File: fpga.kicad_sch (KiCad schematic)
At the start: 50 parts, among them U1 MACHXO2-1200HC-4TG100C, U2 TDC_7200, X1 16MHz

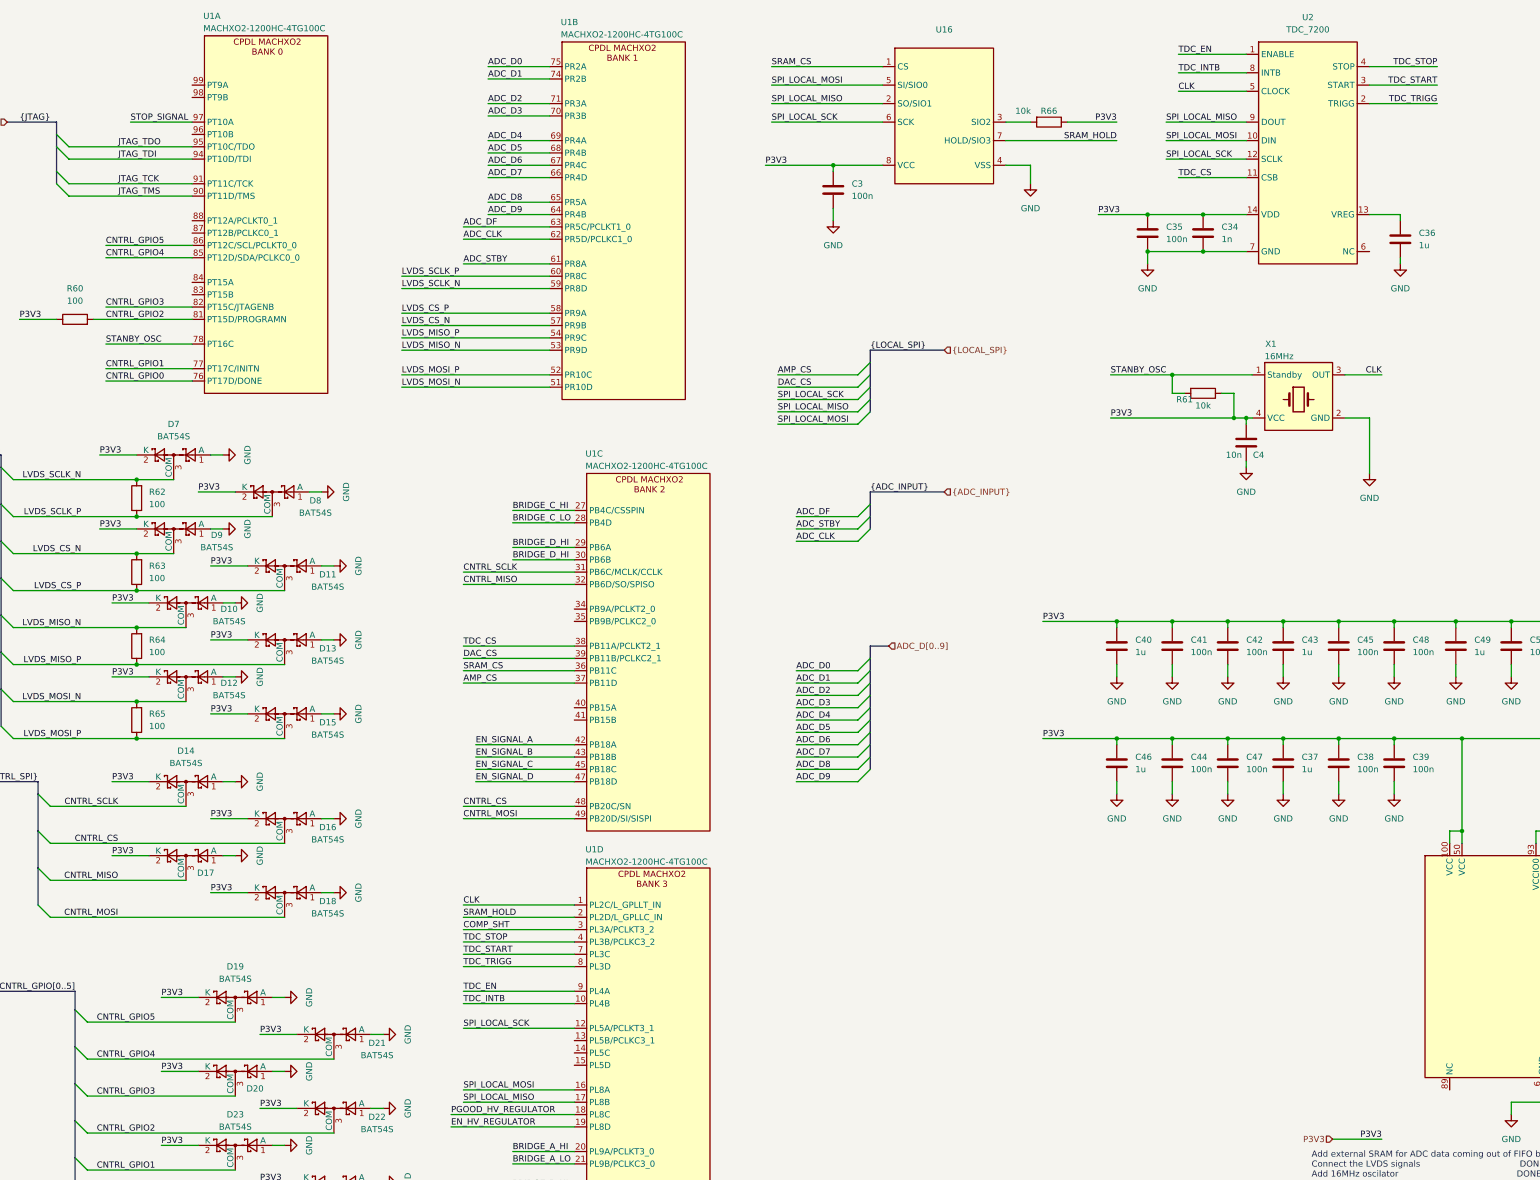
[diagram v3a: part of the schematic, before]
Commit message: schematic ready, basic layout done
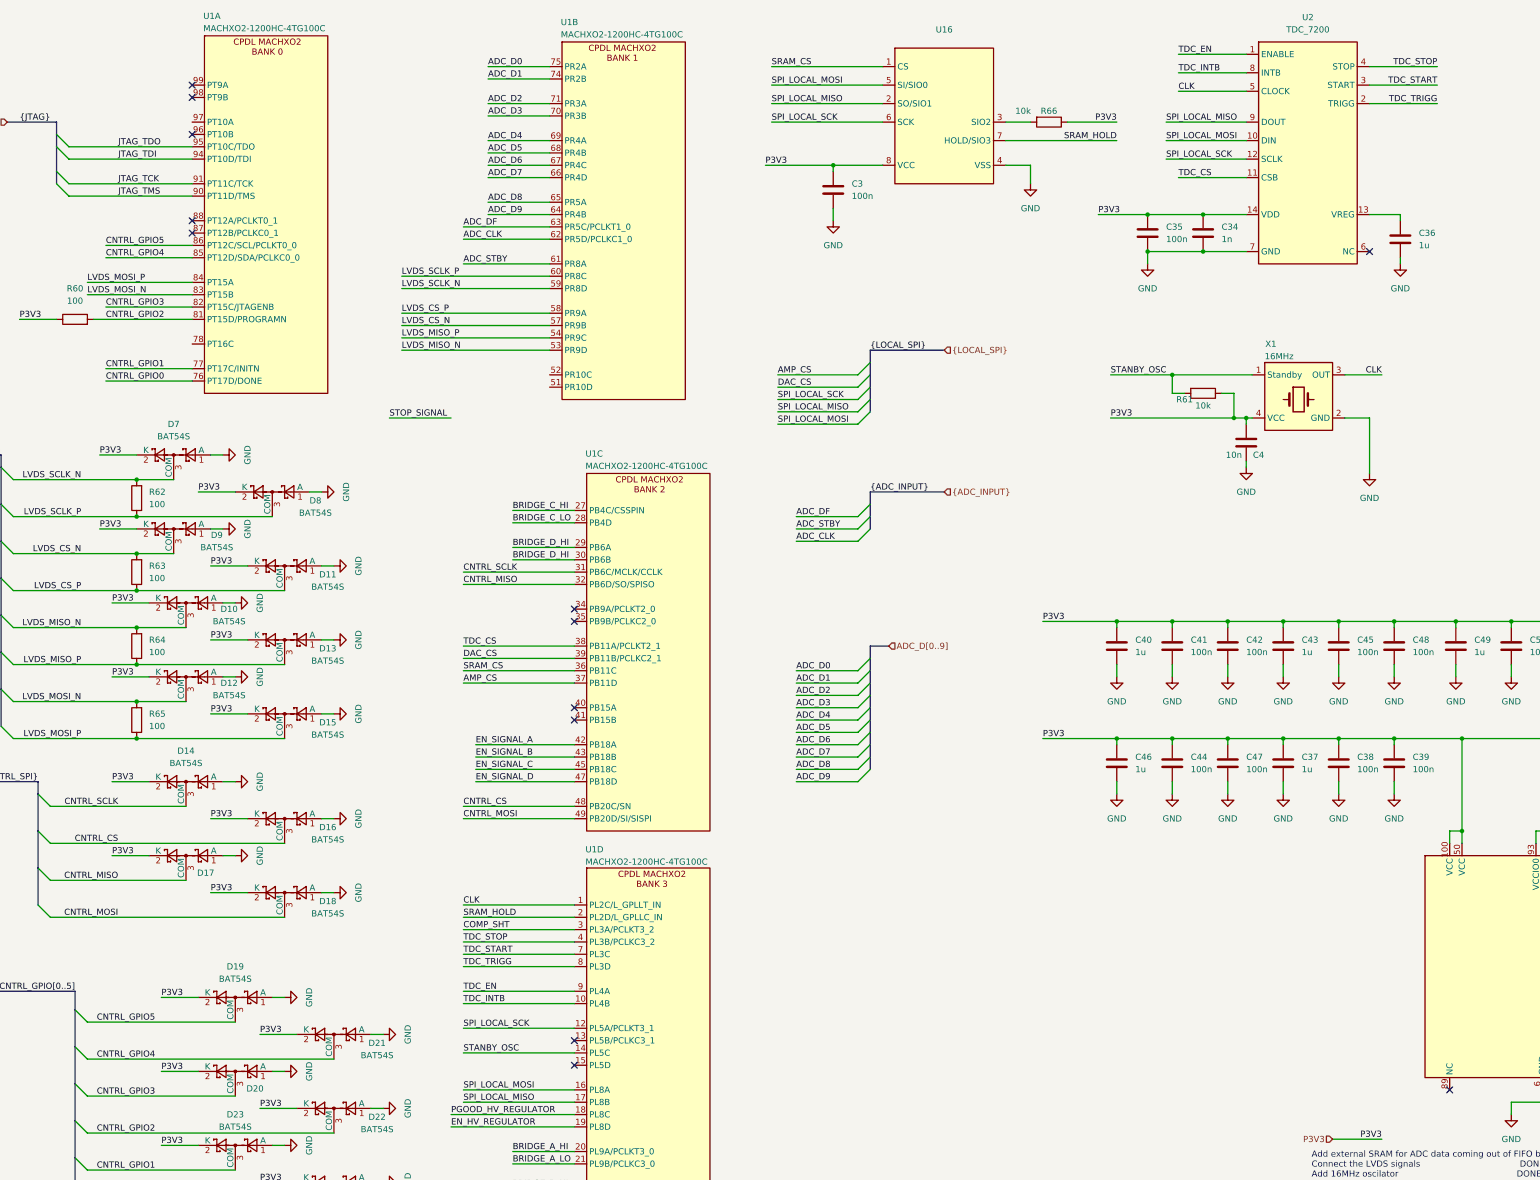
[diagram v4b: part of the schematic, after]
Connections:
- net LVDS_MOSI_N: now also U1.83 (PT15B); no longer U1.51 (PR10D)
- net LVDS_MOSI_P: now also U1.84 (PT15A); no longer U1.52 (PR10C)
- net STANBY_OSC: now also U1.14 (PL5C); no longer U1.78 (PT16C)
- net STOP_SIGNAL: no longer U1.97 (PT10A)
- no-connect marks 0 -> 13
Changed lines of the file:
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@@
 		(color 0 0 0 0)
 	)
+	(no_connect
+		(at 149.86 162.56)
+	)
+	(no_connect
+		(at 71.12 64.77)
+	)
+	(no_connect
+		(at 330.2 241.3)
+	)
+	(no_connect
+		(at 149.86 144.78)
+	)
+	(no_connect
+		(at 71.12 62.23)
+	)
+	(no_connect
+		(at 71.12 36.83)
+	)
+	(no_connect
+		(at 149.86 231.14)
+	)
+	(no_connect
+		(at 149.86 236.22)
+	)
+	(no_connect
+		(at 313.69 68.58)
+	)
+	(no_connect
+		(at 149.86 165.1)
+	)
+	(no_connect
+		(at 71.12 44.45)
+	)
+	(no_connect
+		(at 71.12 34.29)
+	)
+	(no_connect
+		(at 149.86 142.24)
+	)
 	(bus_entry
 		(at 210.82 99.06)
@@
 		)
 	)
+	(wire
+		(pts
+			(xy 49.53 77.47) (xy 71.12 77.47)
+		)
+		(stroke
+			(width 0)
+			(type default)
+		)
+	)
 	(bus
 		(pts
@@
 	(wire
 		(pts
-			(xy 114.3 96.52) (xy 144.78 96.52)
-		)
-		(stroke
-			(width 0)
-			(type default)
-		)
-	)
-	(wire
-		(pts
 			(xy 191.77 104.14) (xy 208.28 104.14)
 		)
@@
 	(wire
 		(pts
-			(xy 58.42 41.91) (xy 71.12 41.91)
-		)
-		(stroke
-			(width 0)
-			(type default)
-		)
-	)
-	(wire
-		(pts
 			(xy 114.3 76.2) (xy 144.78 76.2)
 		)
@@
 	(wire
 		(pts
-			(xy 53.34 87.63) (xy 71.12 87.63)
-		)
-		(stroke
-			(width 0)
-			(type default)
-		)
-	)
-	(wire
-		(pts
 			(xy 360.68 187.96) (xy 360.68 190.5)
 		)
@@
 	(wire
 		(pts
+			(xy 111.76 102.87) (xy 124.46 102.87)
+		)
+		(stroke
+			(width 0)
+			(type default)
+		)
+	)
+	(wire
+		(pts
 			(xy 195.58 125.73) (xy 208.28 125.73)
 		)
@@
 	(wire
 		(pts
-			(xy 365.76 144.78) (xy 365.76 146.05)
+			(xy 127 233.68) (xy 149.86 233.68)
 		)
 		(stroke
@@
 	(wire
 		(pts
-			(xy 114.3 86.36) (xy 144.78 86.36)
+			(xy 365.76 144.78) (xy 365.76 146.05)
 		)
 		(stroke
@@
 	(wire
 		(pts
-			(xy 114.3 93.98) (xy 144.78 93.98)
+			(xy 114.3 86.36) (xy 144.78 86.36)
 		)
 		(stroke
@@
 	(wire
 		(pts
+			(xy 49.53 74.93) (xy 71.12 74.93)
+		)
+		(stroke
+			(width 0)
+			(type default)
+		)
+	)
+	(wire
+		(pts
 			(xy 342.9 144.78) (xy 342.9 146.05)
 		)
@@
 		)
 	)
+	(label "STOP_SIGNAL"
+		(at 111.76 102.87 0)
+		(fields_autoplaced yes)
+		(effects
+			(font
+				(size 1.27 1.27)
+			)
+			(justify left bottom)
+		)
+	)
 	(label "ADC_CLK"
 		(at 127 66.04 0)
@@
 		)
 	)
-	(label "LVDS_MOSI_N"
-		(at 114.3 96.52 0)
-		(fields_autoplaced yes)
-		(effects
-			(font
-				(size 1.27 1.27)
-			)
-			(justify left bottom)
-		)
-	)
 	(label "ADC_D4"
 		(at 132.08 45.72 0)
@@
 		)
 	)
-	(label "STOP_SIGNAL"
-		(at 58.42 41.91 0)
-		(fields_autoplaced yes)
-		(effects
-			(font
-				(size 1.27 1.27)
-			)
-			(justify left bottom)
-		)
-	)
 	(label "{LOCAL_SPI}"
 		(at 210.82 88.9 0)
@@
 		)
 	)
-	(label "LVDS_MOSI_P"
-		(at 114.3 93.98 0)
+	(label "LVDS_MOSI_N"
+		(at 49.53 77.47 0)
 		(fields_autoplaced yes)
 		(effects
@@
 		)
 	)
+	(label "LVDS_MOSI_P"
+		(at 49.53 74.93 0)
+		(fields_autoplaced yes)
+		(effects
+			(font
+				(size 1.27 1.27)
+			)
+			(justify left bottom)
+		)
+	)
 	(label "TDC_INTB"
 		(at 274.32 31.75 0)
@@
 	)
 	(label "STANBY_OSC"
-		(at 53.34 87.63 0)
+		(at 127 233.68 0)
 		(fields_autoplaced yes)
 		(effects
@@
 	)
 	(symbol
+		(lib_name "LCMXO2-1200HC-4TG100C_3")
 		(lib_id "10_ICs:LCMXO2-1200HC-4TG100C")
 		(at 73.66 24.13 0)
@@
 		(pin "3"
 		)
+		(pin "89"
+		)
 		(instances
 			(project "ultrasonic_V3_HW"
@@
 	)
 	(symbol
+		(lib_name "LCMXO2-1200HC-4TG100C_2")
 		(lib_id "10_ICs:LCMXO2-1200HC-4TG100C")
 		(at 152.4 195.58 0)
@@
 		(pin "3"
 		)
+		(pin "89"
+		)
 		(instances

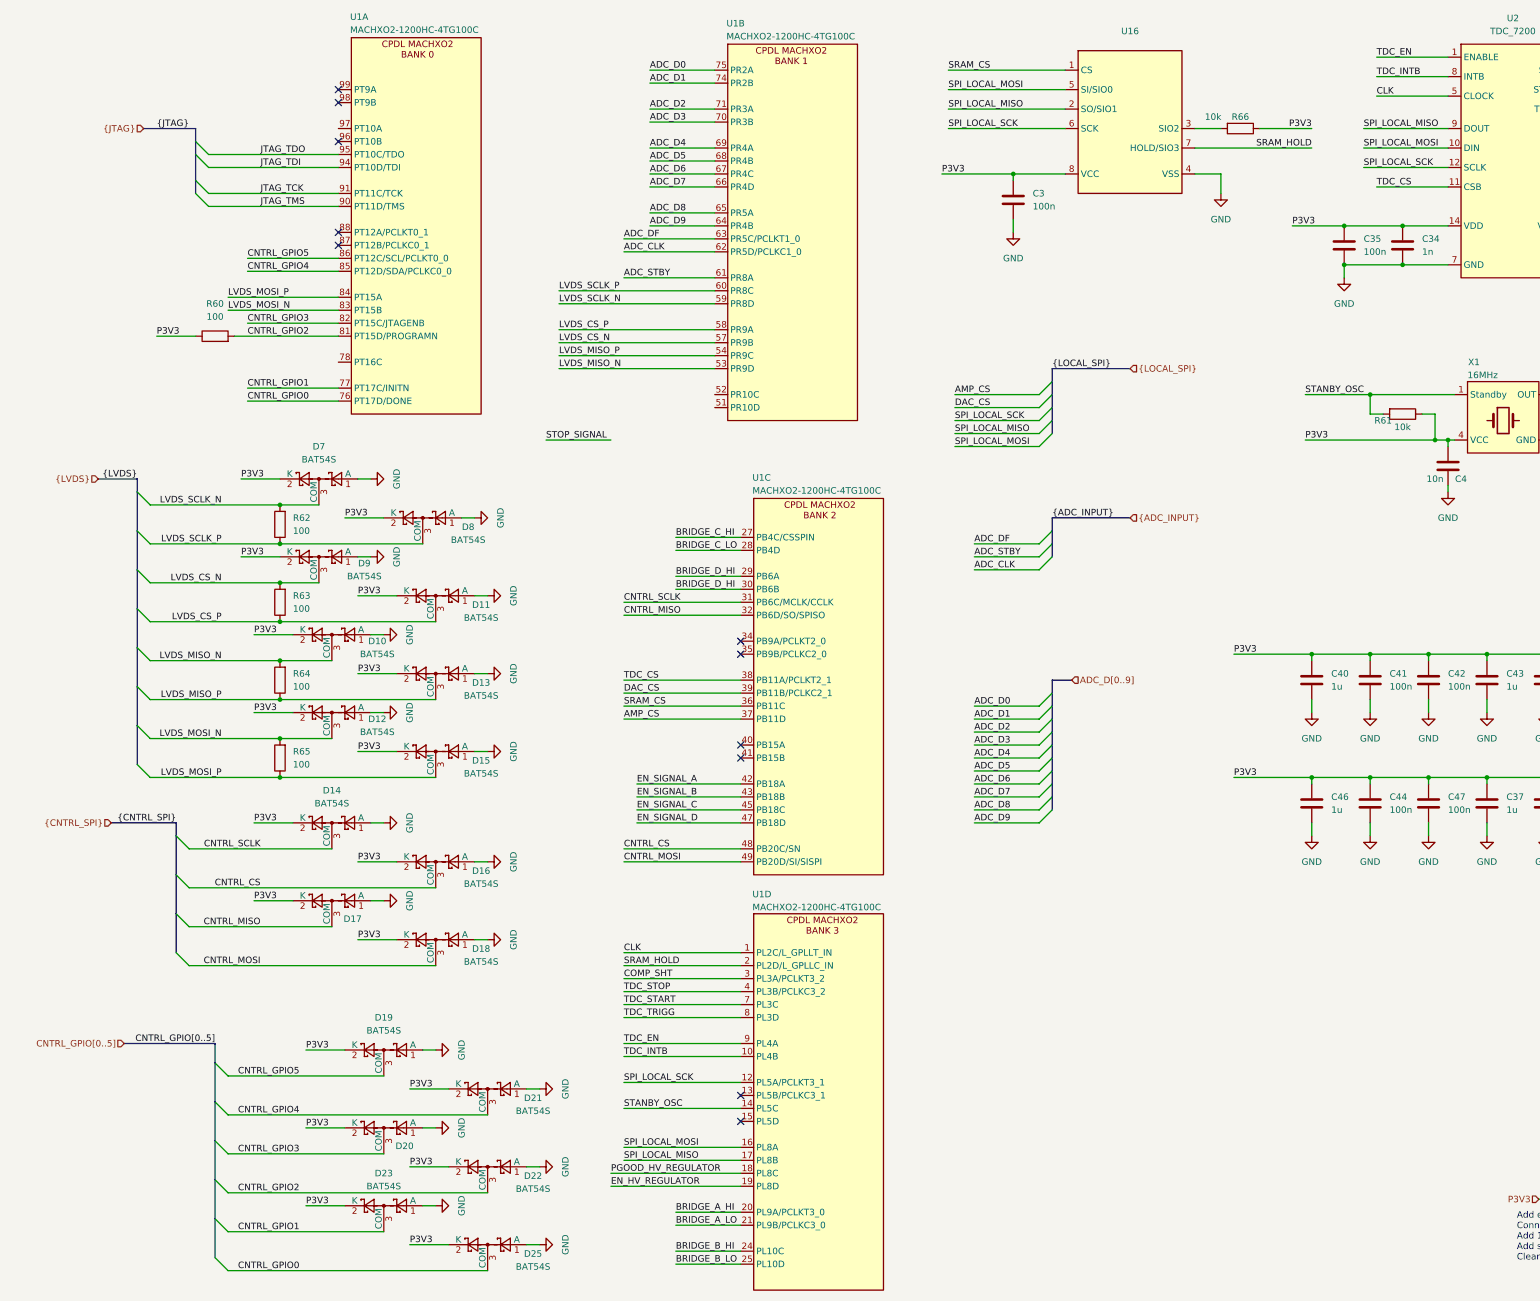
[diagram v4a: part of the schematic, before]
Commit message: changed pins on fpga
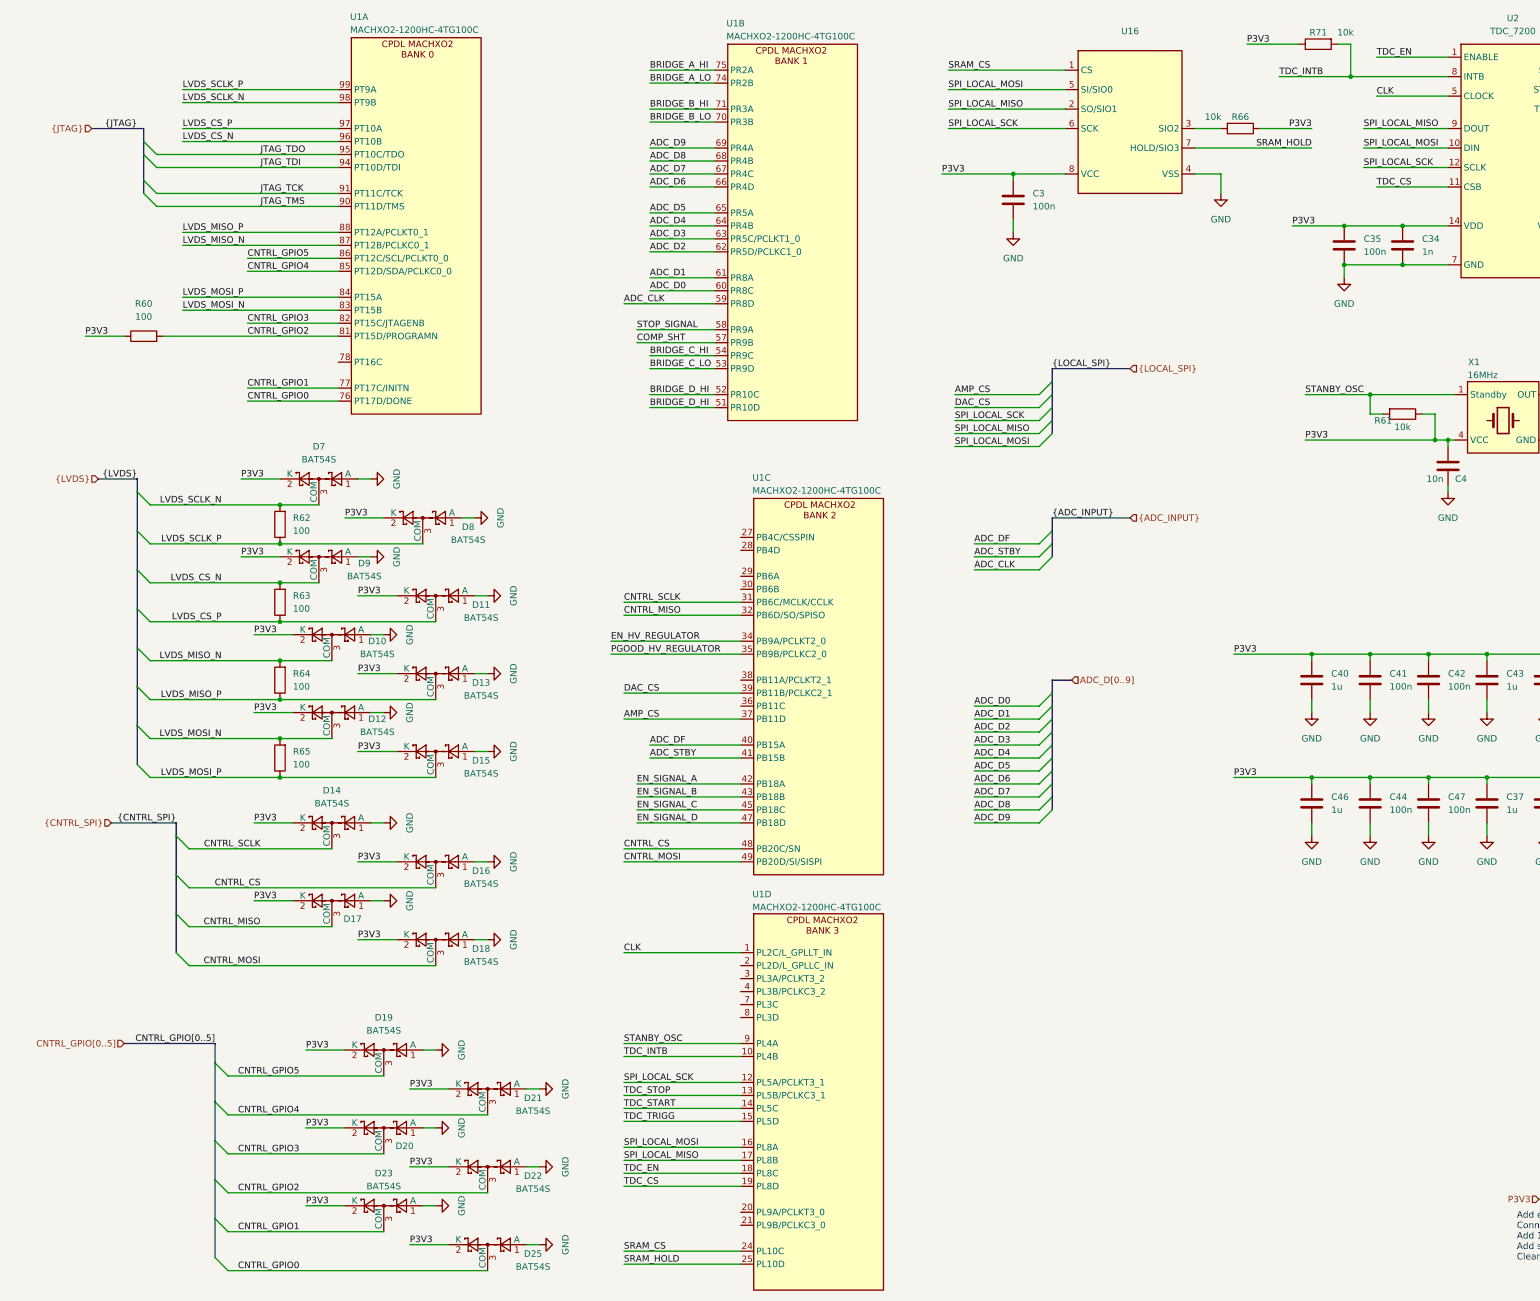
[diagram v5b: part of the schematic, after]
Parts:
- added R71: 10k, Resistor_SMD:R_0603_1608Metric, symbol Device:R
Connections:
- net ADC_CLK: now also U1.59 (PR8D); no longer U1.62 (PR5D/PCLKC1_0)
- net ADC_D0: now also U1.60 (PR8C); no longer U1.75 (PR2A)
- net ADC_D1: now also U1.61 (PR8A); no longer U1.74 (PR2B)
- net ADC_D2: now also U1.62 (PR5D/PCLKC1_0); no longer U1.71 (PR3A)
- net ADC_D3: now also U1.63 (PR5C/PCLKT1_0); no longer U1.70 (PR3B)
- net ADC_D4: now also U1.64 (PR4B); no longer U1.69 (PR4A)
- net ADC_D5: now also U1.65 (PR5A); no longer U1.68 (PR4B)
- net ADC_D6: now also U1.66 (PR4D); no longer U1.67 (PR4C)
- net ADC_D7: now also U1.67 (PR4C); no longer U1.66 (PR4D)
- net ADC_D8: now also U1.68 (PR4B); no longer U1.65 (PR5A)
- net ADC_D9: now also U1.69 (PR4A); no longer U1.64 (PR4B)
- net ADC_DF: now also U1.40 (PB15A); no longer U1.63 (PR5C/PCLKT1_0)
- net ADC_STBY: now also U1.41 (PB15B); no longer U1.61 (PR8A)
- net BRIDGE_A_HI: now also U1.75 (PR2A); no longer U1.20 (PL9A/PCLKT3_0)
- net BRIDGE_A_LO: now also U1.74 (PR2B); no longer U1.21 (PL9B/PCLKC3_0)
- net BRIDGE_B_HI: now also U1.71 (PR3A); no longer U1.24 (PL10C)
- net BRIDGE_B_LO: now also U1.70 (PR3B); no longer U1.25 (PL10D)
- net BRIDGE_C_HI: now also U1.54 (PR9C); no longer U1.27 (PB4C/CSSPIN)
- net BRIDGE_C_LO: now also U1.53 (PR9D); no longer U1.28 (PB4D)
- net BRIDGE_D_HI: now also U1.51 (PR10D), U1.52 (PR10C); no longer U1.29 (PB6A), U1.30 (PB6B)
- net COMP_SHT: now also U1.57 (PR9B); no longer U1.3 (PL3A/PCLKT3_2)
- net EN_HV_REGULATOR: now also U1.34 (PB9A/PCLKT2_0); no longer U1.19 (PL8D)
- net LVDS_CS_N: now also U1.96 (PT10B); no longer U1.57 (PR9B)
- net LVDS_CS_P: now also U1.97 (PT10A); no longer U1.58 (PR9A)
- net LVDS_MISO_N: now also U1.87 (PT12B/PCLKC0_1); no longer U1.53 (PR9D)
- net LVDS_MISO_P: now also U1.88 (PT12A/PCLKT0_1); no longer U1.54 (PR9C)
- net LVDS_SCLK_N: now also U1.98 (PT9B); no longer U1.59 (PR8D)
- net LVDS_SCLK_P: now also U1.99 (PT9A); no longer U1.60 (PR8C)
- net P3V3: now also R71.1
- net PGOOD_HV_REGULATOR: now also U1.35 (PB9B/PCLKC2_0); no longer U1.18 (PL8C)
- net SRAM_CS: now also U1.24 (PL10C); no longer U1.36 (PB11C)
- net SRAM_HOLD: now also U1.25 (PL10D); no longer U1.2 (PL2D/L_GPLLC_IN)
- net STANBY_OSC: now also U1.9 (PL4A); no longer U1.14 (PL5C)
- net STOP_SIGNAL: now also U1.58 (PR9A)
- net TDC_CS: now also U1.19 (PL8D); no longer U1.38 (PB11A/PCLKT2_1)
- net TDC_EN: now also U1.18 (PL8C); no longer U1.9 (PL4A)
- net TDC_INTB: now also R71.2
- net TDC_START: now also U1.14 (PL5C); no longer U1.7 (PL3C)
- net TDC_STOP: now also U1.13 (PL5B/PCLKC3_1); no longer U1.4 (PL3B/PCLKC3_2)
- net TDC_TRIGG: now also U1.15 (PL5D); no longer U1.8 (PL3D)
- no-connect marks 13 -> 2
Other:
- moved on the sheet: R60
